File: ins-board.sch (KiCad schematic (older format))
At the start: 48 parts, among them P1 CONN_8, P2 PWR, U1 STM32F042C6T6, U2 MIC5201-3.3YS, U3 H3LIS331DL, U4 MPU6000, U5 LPS331AP, X1 CRYSTAL 16MHz 10ppm

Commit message: Generate netlist
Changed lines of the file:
@@
 Connection ~ 2000 3700
 Wire Wire Line
-	1050 1900 1150 1900
-Wire Wire Line
-	1150 1900 1250 1900
+	1050 1900 1250 1900
 Wire Wire Line
 	1050 1800 1050 1900
 Wire Wire Line
-	1000 1400 1050 1400
-Wire Wire Line
-	1050 1400 1250 1400
-Wire Wire Line
-	3950 5500 4250 5500
-Wire Wire Line
-	4250 5500 4450 5500
-Wire Wire Line
-	4800 5500 4800 5800
-Wire Wire Line
-	4800 5800 4800 6100
-Wire Wire Line
-	1800 4100 2000 4100
-Wire Wire Line
-	2000 4100 2450 4100
+	1000 1400 1250 1400
+Wire Wire Line
+	3950 5500 4450 5500
+Wire Wire Line
+	4800 5500 4800 6100
+Wire Wire Line
+	1800 4100 2450 4100
 Wire Wire Line
 	1200 7100 1200 7000
@@
 Connection ~ 2450 2400
 Wire Wire Line
-	2450 2800 2450 2900
-Wire Wire Line
-	2450 2900 2450 3000
+	2450 2800 2450 3000
 Wire Wire Line
 	1650 2400 1650 2250
@@
 	1800 4100 1800 4200
 Wire Wire Line
-	2100 1700 2200 1700
-Wire Wire Line
-	2200 1700 2450 1700
+	2100 1700 2450 1700
 Wire Wire Line
 	950  7100 950  7150
@@
 	1200 6700 1200 6800
 Wire Wire Line
-	800  7100 950  7100
-Wire Wire Line
-	950  7100 1050 7100
-Wire Wire Line
-	1050 7100 1200 7100
+	800  7100 1200 7100
 Connection ~ 950  7100
 Wire Wire Line
-	4450 5800 4800 5800
-Wire Wire Line
-	4800 5800 4950 5800
+	4450 5800 4950 5800
 Connection ~ 4800 5800
 Wire Wire Line
-	4050 6100 4250 6100
-Wire Wire Line
-	4250 6100 4450 6100
+	4050 6100 4450 6100
 Wire Wire Line
 	3250 1200 3250 1350
@@
 	3350 1250 3450 1250
 Wire Wire Line
-	700  6700 800  6700
-Wire Wire Line
-	800  6700 1050 6700
-Wire Wire Line
-	1050 6700 1200 6700
-Wire Wire Line
-	1250 1200 1250 1400
-Wire Wire Line
-	1250 1400 1250 1500
+	700  6700 1200 6700
+Wire Wire Line
+	1250 1200 1250 1500
 Connection ~ 1150 1900
 Wire Wire Line
@@
 	4900 3600 4900 3750
 Wire Wire Line
-	4700 3600 4800 3600
-Wire Wire Line
-	4800 3600 4900 3600
+	4700 3600 4900 3600
 Connection ~ 1050 6700
 Connection ~ 800  6700
@@
 $EndComp
 Wire Wire Line
-	4450 5750 4450 5800
-Wire Wire Line
-	4450 5800 4450 5850
+	4450 5750 4450 5850
 Connection ~ 4450 5800
 $Comp
@@
 Connection ~ 7850 3950
 Wire Wire Line
-	7800 3950 7850 3950
-Wire Wire Line
-	7850 3950 8400 3950
+	7800 3950 8400 3950
 Wire Wire Line
 	7550 3850 8400 3850
@@
 	8400 4050 8000 4050
 Wire Wire Line
-	7850 4300 7850 4350
-Wire Wire Line
-	7850 4350 7850 4450
+	7850 4300 7850 4450
 Wire Wire Line
 	7250 3850 7250 3950
@@
 $EndComp
 Wire Wire Line
-	5900 1000 6000 1000
-Wire Wire Line
-	6000 1000 6450 1000
-Wire Wire Line
-	6000 1000 6000 1100
-Wire Wire Line
-	6000 1100 6000 1150
+	5900 1000 6450 1000
+Wire Wire Line
+	6000 1000 6000 1150
 Connection ~ 6000 1000
 $Comp
@@
 $EndComp
 Wire Wire Line
-	7000 1900 7100 1900
-Wire Wire Line
-	7100 1900 7150 1900
-Wire Wire Line
-	7150 1900 7200 1900
-Wire Wire Line
-	7200 1900 7300 1900
+	7000 1900 7300 1900
 Wire Wire Line
 	7150 2000 7150 1900
@@
 $EndComp
 Wire Wire Line
-	5750 1500 5900 1500
-Wire Wire Line
-	5900 1500 6000 1500
+	5750 1500 6000 1500
 Wire Wire Line
 	5750 1100 6000 1100
@@
 $EndComp
 Wire Wire Line
-	10300 4350 10400 4350
-Wire Wire Line
-	10400 4350 10700 4350
+	10300 4350 10700 4350
 $Comp
 L GND #PWR027
@@
 $EndComp
 Wire Wire Line
-	6000 2650 6100 2650
-Wire Wire Line
-	6100 2650 6150 2650
+	6000 2650 6150 2650
 $Comp
 L VCC #PWR029
@@
 VCC_A
 Wire Wire Line
-	7450 2650 7550 2650
-Wire Wire Line
-	7550 2650 7650 2650
-Wire Wire Line
-	7650 2650 7800 2650
-Wire Wire Line
-	7800 2650 7950 2650
+	7450 2650 7950 2650
 Connection ~ 7650 2650
 Wire Wire Line
@@
 	7550 3100 7550 3000
 Wire Wire Line
-	2450 2400 2450 2300
-Wire Wire Line
-	2450 2300 2450 2200
-Wire Wire Line
-	2450 2200 2450 2000
+	2450 2400 2450 2000
 Connection ~ 2450 2800
 Connection ~ 2450 2900
@@
 Connection ~ 4800 3600
 Wire Wire Line
-	1550 2800 1650 2800
-Wire Wire Line
-	1650 2800 1800 2800
-Wire Wire Line
-	1800 2800 2050 2800
-Wire Wire Line
-	2050 2800 2300 2800
-Wire Wire Line
-	2300 2800 2450 2800
-Wire Wire Line
-	1550 2400 1650 2400
-Wire Wire Line
-	1650 2400 1800 2400
-Wire Wire Line
-	1800 2400 2050 2400
-Wire Wire Line
-	2050 2400 2300 2400
-Wire Wire Line
-	2300 2400 2450 2400
+	1550 2800 2450 2800
+Wire Wire Line
+	1550 2400 2450 2400
 NoConn ~ 7850 1350
 $Comp
@@
 	1500 6000 1500 5850
 Wire Wire Line
-	1500 5850 1650 5850
-Wire Wire Line
-	1650 5850 1800 5850
-Wire Wire Line
-	1800 5850 1950 5850
-Wire Wire Line
-	1950 5850 2100 5850
-Wire Wire Line
-	2100 5850 2250 5850
-Wire Wire Line
-	2250 5800 2250 5850
-Wire Wire Line
-	2250 5850 2250 6000
+	1500 5850 2250 5850
+Wire Wire Line
+	2250 5800 2250 6000
 Connection ~ 2250 5850
 Wire Wire Line
@@
 	8800 1750 8800 1700
 Wire Wire Line
-	8800 1350 9100 1350
-Wire Wire Line
-	9100 1350 9150 1350
-Wire Wire Line
-	9100 1050 9100 1150
-Wire Wire Line
-	9100 1150 9100 1250
-Wire Wire Line
-	9100 1250 9100 1350
+	8800 1350 9150 1350
+Wire Wire Line
+	9100 1050 9100 1350
 Wire Wire Line
 	9100 1250 9150 1250
@@
 	9150 1750 9100 1750
 Wire Wire Line
-	9100 1750 9100 1950
-Wire Wire Line
-	9100 1950 9100 2050
-Wire Wire Line
-	9100 2050 9100 2150
-Wire Wire Line
-	9100 2150 9100 2250
-Wire Wire Line
-	9100 2250 9100 2300
+	9100 1750 9100 2300
 Wire Wire Line
 	9100 2250 9150 2250
@@
 	10350 4250 10350 4150
 Wire Wire Line
-	10300 4150 10350 4150
-Wire Wire Line
-	10350 4150 10450 4150
+	10300 4150 10450 4150
 Wire Wire Line
 	10450 4150 10450 4200
@@
 	2000 4050 2000 4100
 Wire Wire Line
-	1800 3700 2000 3700
-Wire Wire Line
-	2000 3700 2450 3700
+	1800 3700 2450 3700
 $EndSCHEMATC

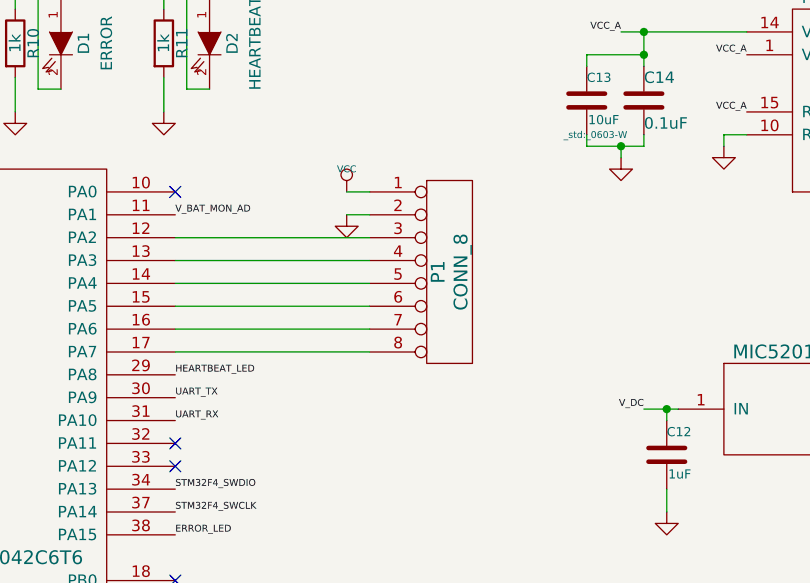
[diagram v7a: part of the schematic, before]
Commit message: Replace components to ease routing
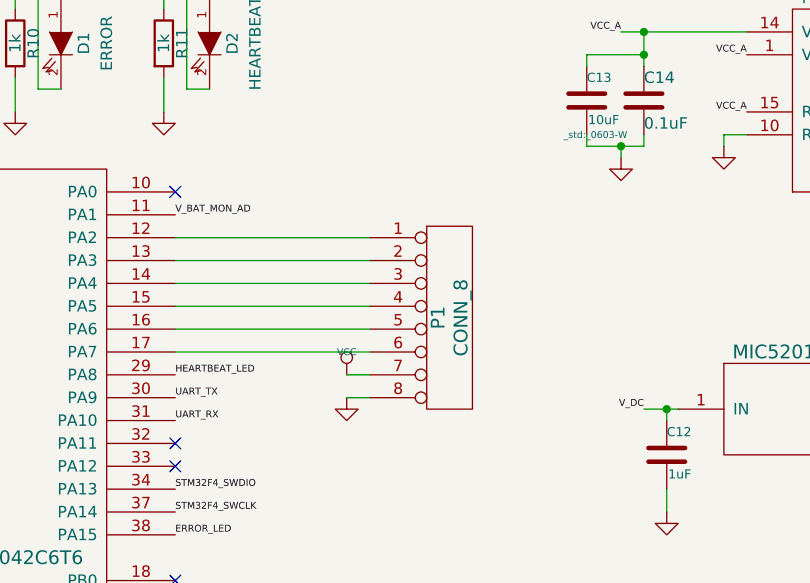
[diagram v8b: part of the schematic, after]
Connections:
- net GND: now also P1.8 (P8); no longer P1.2 (P2)
- net VCC: now also P1.7 (P7); no longer P1.1 (P1)
- net at U1.12 (PA2): now also P1.1 (P1); no longer P1.3 (P3)
- net at U1.13 (PA3): now also P1.2 (P2); no longer P1.4 (P4)
- net at U1.14 (PA4): now also P1.3 (P3); no longer P1.5 (P5)
- net at U1.15 (PA5): now also P1.4 (P4); no longer P1.6 (P6)
- net at U1.16 (PA6): now also P1.5 (P5); no longer P1.7 (P7)
- net at U1.17 (PA7): now also P1.6 (P6); no longer P1.8 (P8)
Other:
- moved on the sheet: P1
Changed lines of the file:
@@
 L CONN_8 P1
 U 1 1 551457FA
-P 5150 2050
-F 0 "P1" V 5100 2050 60  0000 C CNN
-F 1 "CONN_8" V 5200 2050 60  0000 C CNN
-F 2 "_connectors:_Solder_Pad1.27_8" H 5150 2050 60  0001 C CNN
-F 3 "" H 5150 2050 60  0000 C CNN
-	1    5150 2050
+P 5150 2250
+F 0 "P1" V 5100 2250 60  0000 C CNN
+F 1 "CONN_8" V 5200 2250 60  0000 C CNN
+F 2 "_connectors:_Solder_Pad1.27_8" H 5150 2250 60  0001 C CNN
+F 3 "" H 5150 2250 60  0000 C CNN
+	1    5150 2250
 	1    0    0    -1
 $EndComp
@@
 L VCC #PWR038
 U 1 1 55145879
-P 4700 1700
-F 0 "#PWR038" H 4700 1800 30  0001 C CNN
-F 1 "VCC" H 4700 1800 30  0000 C CNN
-F 2 "" H 4700 1700 60  0000 C CNN
-F 3 "" H 4700 1700 60  0000 C CNN
-	1    4700 1700
-	1    0    0    -1
-$EndComp
-Wire Wire Line
-	4700 1700 4800 1700
+P 4700 2500
+F 0 "#PWR038" H 4700 2600 30  0001 C CNN
+F 1 "VCC" H 4700 2600 30  0000 C CNN
+F 2 "" H 4700 2500 60  0000 C CNN
+F 3 "" H 4700 2500 60  0000 C CNN
+	1    4700 2500
+	1    0    0    -1
+$EndComp
 $Comp
 L GND #PWR039
 U 1 1 55145B0D
-P 4700 1800
-F 0 "#PWR039" H 4700 1800 30  0001 C CNN
-F 1 "GND" H 4700 1730 30  0001 C CNN
-F 2 "" H 4700 1800 60  0000 C CNN
-F 3 "" H 4700 1800 60  0000 C CNN
-	1    4700 1800
-	1    0    0    -1
-$EndComp
-Wire Wire Line
-	4700 1800 4800 1800
+P 4700 2600
+F 0 "#PWR039" H 4700 2600 30  0001 C CNN
+F 1 "GND" H 4700 2530 30  0001 C CNN
+F 2 "" H 4700 2600 60  0000 C CNN
+F 3 "" H 4700 2600 60  0000 C CNN
+	1    4700 2600
+	1    0    0    -1
+$EndComp
 Wire Wire Line
 	4800 1900 3950 1900
@@
 Wire Wire Line
 	1800 3700 2450 3700
+Wire Wire Line
+	4800 2500 4700 2500
+Wire Wire Line
+	4700 2600 4800 2600
 $EndSCHEMATC
